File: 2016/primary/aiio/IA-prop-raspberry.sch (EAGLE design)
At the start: 94 parts, among them U1 ARDUINO_R3_SHIELD

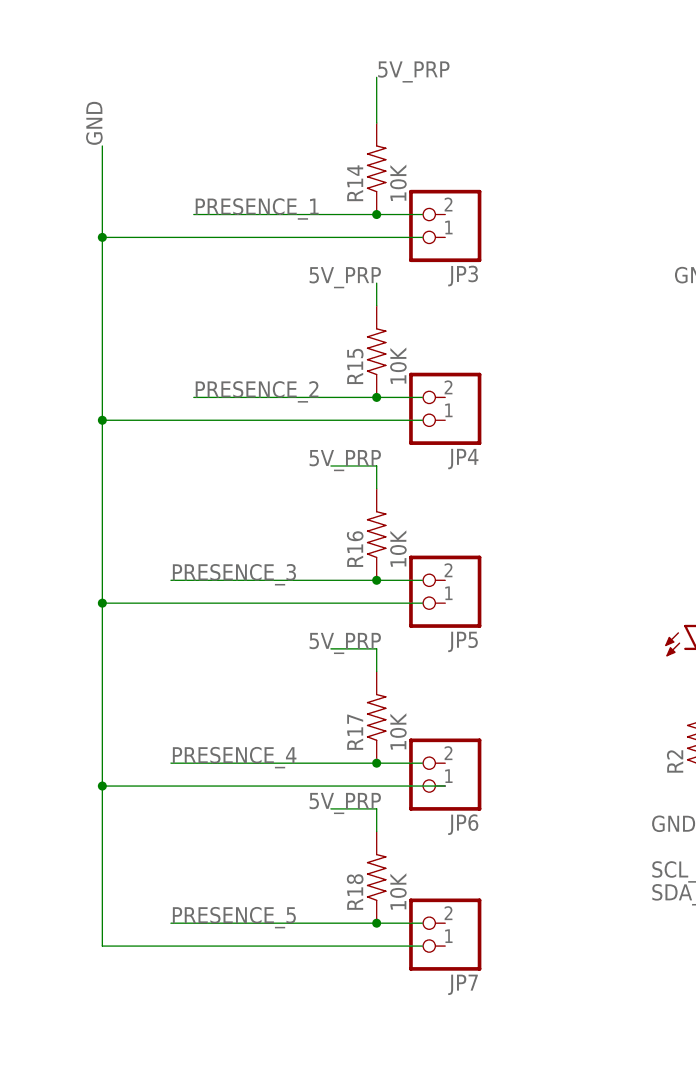
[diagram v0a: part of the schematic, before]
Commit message: [AIIO_boards] Route presence connectors.
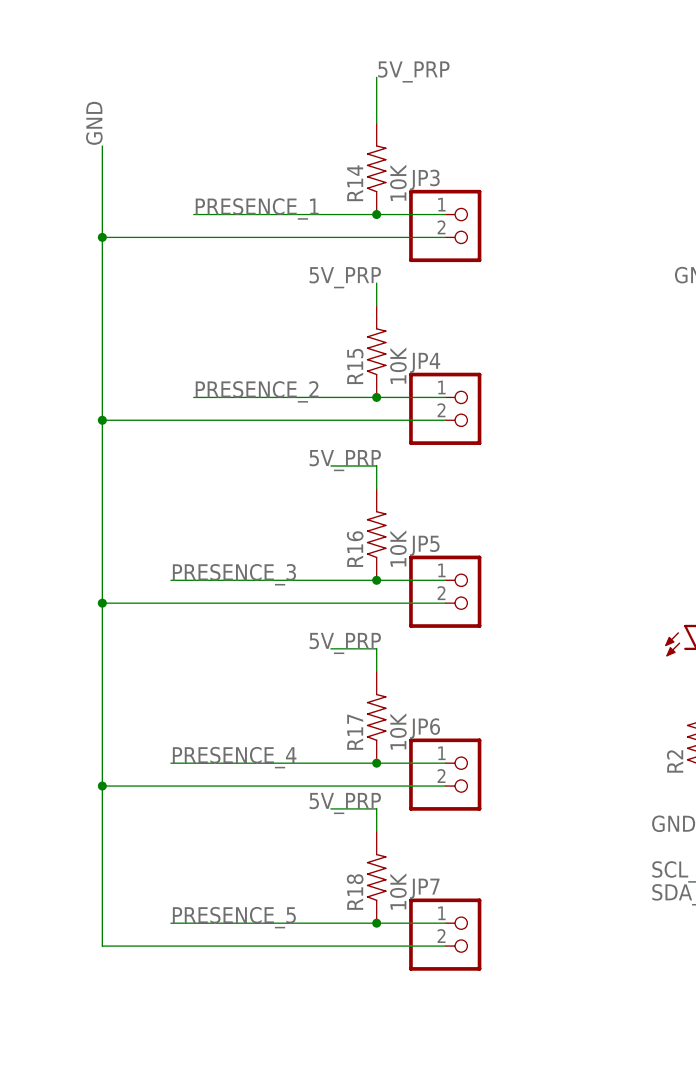
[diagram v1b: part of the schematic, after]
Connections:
- net GND: now also JP3.2, JP4.2, JP5.2, JP6.2, JP7.2; no longer JP6.1
- net PRESENCE_1: now also JP3.1
- net PRESENCE_2: now also JP4.1
- net PRESENCE_3: now also JP5.1
- net PRESENCE_4: now also JP6.1
- net PRESENCE_5: now also JP7.1
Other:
- moved on the sheet: JP3, JP4, JP5, JP6, JP7

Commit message: [AIIO_board] Add I2C and UART connectors to Arduino and RP2 boards.
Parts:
- removed ARD_BLUETOOTH: (no value), con-lstb:MA04-1
- removed CON_I2C_UART: (no value), con-lsta:FE06-1
- removed RST_RP2: (no value), SparkFun:TAC_SWITCHPTH
- added 12V_PROPU_SRC2, 12V_PROPU_SRC3, 5V_SIG, 5V_SIG2, 5V_SIG3: (no value), con-ptr500:AK300/2
- added CON_I2CARDU, CON_I2CARDU_1, CON_I2CRP2, CON_I2CRP2_2, CON_I2C_SERVOS, CON_I2C_SONARS, CON_UARTARDU, CON_UARTRP2: (no value), pinhead:PINHD-1X4
- added JP8, JP9, JP_5VSIG, JP_GND_5VSIG: (no value), pinhead:PINHD-1X3
- JP1, JP2: device SparkFun:M05PTH -> pinhead:PINHD-1X3
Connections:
- net 5V_SAL renamed 5V_PWR
- removed net N$11: 12V_PROPU_SRC-1.KL, 12V_PROPU_SRC1-1.KL, LED4.A, U$6.P$2
- removed net N$48: RP2.RUN1, RST_RP2.1
- removed net SCL_RP2: RP2.SCL, SV1.3, SV10.3, SV11.3, SV12.3, SV2.3, SV3.3, SV4.3, SV5.3, SV6.3, SV7.3, SV8.3, SV9-1.3, SV9.3
- removed net SDA_RP2: RP2.SDA, SV1.4, SV10.4, SV11.4, SV12.4, SV2.4, SV3.4, SV4.4, SV5.4, SV6.4, SV7.4, SV8.4, SV9-1.4, SV9.4
- new net 5VI2CARDU: CON_I2CARDU.4, CON_I2CARDU_1.4, JP9.3
- new net 5VI2CRP2: CON_I2CRP2.4, CON_I2CRP2_2.4, JP8.3
- new net 5VSIG: R13.2
- new net 5VSIG_SERVOS: CON_I2C_SERVOS.4, R4.2, R7.2, U$1.VDD
- new net 5VUARTRP2: CON_UARTRP2.4, JP2.1
- new net 5V_SIG: 5V_SIG-2.KL, 5V_SIG2-2.KL, 5V_SIG3-2.KL, C4.+, JP1.2, JP2.2, JP8.2, JP9.2, JP_5VSIG.1, JP_5VSIG.2, JP_5VSIG.3, LED1.A, R11.2, R12.2, R14.2, R5.1, RP2.5V0A, U$2.+VOUT, U1.5V
- new net 5V_SONARS: CON_I2C_SONARS.4, SV1.5, SV10.5, SV11.5, SV12.5, SV2.5, SV3.5, SV4.5, SV5.5, SV6.5, SV7.5, SV8.5, SV9-1.5, SV9.5
- new net GND1: CON_I2CRP2.3, CON_I2CRP2_2.3, R2.1
- new net GND2: CON_I2CARDU.3, CON_I2CARDU_1.3, U1.GND@0, U1.GND@1, U1.GND@2
- new net GND_SONARS: CON_I2C_SONARS.3, SV1.1, SV10.1, SV11.1, SV12.1, SV2.1, SV3.1, SV4.1, SV5.1, SV6.1, SV7.1, SV8.1, SV9-1.1, SV9.1
- new net N$40: 12V_PROPU_SRC-1.KL, 12V_PROPU_SRC1-1.KL, 12V_PROPU_SRC2-1.KL, 12V_PROPU_SRC3-1.KL, LED4.A, U$6.P$2
- new net SCL_RP1: CON_I2CRP2.1, CON_I2CRP2_2.1, RP2.SCL
- new net SCL_SERVOS: CON_I2C_SERVOS.1, P-UP_SCL.2, U$1.SCL
- new net SCL_SONARS: CON_I2C_SONARS.2, SV1.3, SV10.3, SV11.3, SV12.3, SV2.3, SV3.3, SV4.3, SV5.3, SV6.3, SV7.3, SV8.3, SV9-1.3, SV9.3
- new net SDA_RP1: CON_I2CRP2.2, CON_I2CRP2_2.2, RP2.SDA
- new net SDA_SERVOS: CON_I2C_SERVOS.2, P-UP_SDA.1, U$1.SDA
- new net SDA_SONARS: CON_I2C_SONARS.1, SV1.4, SV10.4, SV11.4, SV12.4, SV2.4, SV3.4, SV4.4, SV5.4, SV6.4, SV7.4, SV8.4, SV9-1.4, SV9.4
- net 5V_PRP: no longer ARD_BLUETOOTH.1, C4.+, CON_I2C_UART.1, JP1.1, JP1.2, JP1.3, JP1.4, JP1.5, LED1.A, R11.2, R12.2, R13.2, R14.2, R4.2, R5.1, R7.2, RP2.5V0A, SV1.5, SV10.5, SV11.5, SV12.5, SV2.5, SV3.5, SV4.5, SV5.5, SV6.5, SV7.5, SV8.5, SV9-1.5, SV9.5, U$1.VDD, U$2.+VOUT, U1.5V
- net ARD_RX: now also CON_UARTARDU.1; no longer ARD_BLUETOOTH.3
- net ARD_TX: now also CON_UARTARDU.2; no longer ARD_BLUETOOTH.4
- net BAT_12V_PROPU-: now also 12V_PROPU_SRC2-2.KL, 12V_PROPU_SRC3-2.KL
- net GND: now also 5V_SIG-1.KL, 5V_SIG2-1.KL, 5V_SIG3-1.KL, CON_I2C_SERVOS.3, CON_UARTARDU.3, CON_UARTRP2.3, JP_GND_5VSIG.1, JP_GND_5VSIG.2, JP_GND_5VSIG.3; no longer ARD_BLUETOOTH.2, CON_I2C_UART.2, JP2.1, JP2.2, JP2.3, JP2.4, JP2.5, R2.1, SV1.1, SV10.1, SV11.1, SV12.1, SV2.1, SV3.1, SV4.1, SV5.1, SV6.1, SV7.1, SV8.1, SV9-1.1, SV9.1, U1.GND@0, U1.GND@1, U1.GND@2
- net N$1: now also CON_UARTARDU.4, JP1.1; no longer RP2.RUN2, RST_RP2.3
- net RX_RP2: now also CON_UARTRP2.1; no longer CON_I2C_UART.6
- net SCL_ARDU: now also CON_I2CARDU.1, CON_I2CARDU_1.1; no longer CON_I2C_UART.4, P-UP_SCL.2, U$1.SCL
- net SDA_ARDU: now also CON_I2CARDU.2, CON_I2CARDU_1.2; no longer CON_I2C_UART.3, P-UP_SDA.1, U$1.SDA
- net TX_RP2: now also CON_UARTRP2.2; no longer CON_I2C_UART.5
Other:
- moved on the sheet: 12V_BOARDS1-1, 12V_BOARDS1-2, C3, C4, IHM, LED1, LED2, LED3, P-UP_SCL, P-UP_SDA, PWR_RP2, R1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

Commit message: [AIIO_board] Route IHM components.
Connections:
- removed net GND2: CON_I2CARDU.3, CON_I2CARDU_1.3, U1.GND@0, U1.GND@1, U1.GND@2
- removed net GND_SONARS: CON_I2C_SONARS.3, SV1.1, SV10.1, SV11.1, SV12.1, SV2.1, SV3.1, SV4.1, SV5.1, SV6.1, SV7.1, SV8.1, SV9-1.1, SV9.1
- net GND: now also CON_I2CARDU.3, CON_I2CARDU_1.3, CON_I2C_SONARS.3, SV1.1, SV10.1, SV11.1, SV12.1, SV2.1, SV3.1, SV4.1, SV5.1, SV6.1, SV7.1, SV8.1, SV9-1.1, SV9.1, U1.GND@0, U1.GND@1, U1.GND@2
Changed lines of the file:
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@@
 <label x="269.24" y="-91.44" size="1.778" layer="95"/>
+</segment>
+<segment>
+<pinref part="SV3" gate="G$1" pin="1"/>
+<wire x1="320.04" y1="55.88" x2="322.58" y2="55.88" width="0.1524" layer="91"/>
+<wire x1="322.58" y1="55.88" x2="322.58" y2="30.48" width="0.1524" layer="91"/>
+<pinref part="SV2" gate="G$1" pin="1"/>
+<wire x1="322.58" y1="30.48" x2="322.58" y2="2.54" width="0.1524" layer="91"/>
+<wire x1="322.58" y1="2.54" x2="322.58" y2="-25.4" width="0.1524" layer="91"/>
+<wire x1="322.58" y1="-25.4" x2="322.58" y2="-43.18" width="0.1524" layer="91"/>
+<wire x1="294.64" y1="55.88" x2="297.18" y2="55.88" width="0.1524" layer="91"/>
+<wire x1="297.18" y1="55.88" x2="297.18" y2="30.48" width="0.1524" layer="91"/>
+<wire x1="297.18" y1="30.48" x2="297.18" y2="2.54" width="0.1524" layer="91"/>
+<wire x1="297.18" y1="2.54" x2="297.18" y2="-25.4" width="0.1524" layer="91"/>
+<wire x1="297.18" y1="-25.4" x2="297.18" y2="-43.18" width="0.1524" layer="91"/>
+<wire x1="322.58" y1="-43.18" x2="297.18" y2="-43.18" width="0.1524" layer="91"/>
+<pinref part="SV1" gate="G$1" pin="1"/>
+<wire x1="269.24" y1="55.88" x2="271.78" y2="55.88" width="0.1524" layer="91"/>
+<wire x1="271.78" y1="55.88" x2="271.78" y2="30.48" width="0.1524" layer="91"/>
+<pinref part="SV4" gate="G$1" pin="1"/>
+<wire x1="271.78" y1="30.48" x2="271.78" y2="2.54" width="0.1524" layer="91"/>
+<wire x1="271.78" y1="2.54" x2="271.78" y2="-25.4" width="0.1524" layer="91"/>
+<wire x1="271.78" y1="-25.4" x2="271.78" y2="-43.18" width="0.1524" layer="91"/>
+<wire x1="269.24" y1="30.48" x2="271.78" y2="30.48" width="0.1524" layer="91"/>
+<junction x="271.78" y="30.48"/>
+<pinref part="SV7" gate="G$1" pin="1"/>
+<wire x1="269.24" y1="2.54" x2="271.78" y2="2.54" width="0.1524" layer="91"/>
+<junction x="271.78" y="2.54"/>
+<pinref part="SV10" gate="G$1" pin="1"/>
+<wire x1="269.24" y1="-25.4" x2="271.78" y2="-25.4" width="0.1524" layer="91"/>
+<junction x="271.78" y="-25.4"/>
+<wire x1="297.18" y1="-43.18" x2="271.78" y2="-43.18" width="0.1524" layer="91"/>
+<junction x="297.18" y="-43.18"/>
+<wire x1="271.78" y1="-43.18" x2="261.62" y2="-43.18" width="0.1524" layer="91"/>
+<junction x="271.78" y="-43.18"/>
+<label x="251.46" y="-43.18" size="1.778" layer="95"/>
+<pinref part="SV5" gate="G$1" pin="1"/>
+<wire x1="294.64" y1="30.48" x2="297.18" y2="30.48" width="0.1524" layer="91"/>
+<junction x="297.18" y="30.48"/>
+<pinref part="SV8" gate="G$1" pin="1"/>
+<wire x1="294.64" y1="2.54" x2="297.18" y2="2.54" width="0.1524" layer="91"/>
+<junction x="297.18" y="2.54"/>
+<pinref part="SV6" gate="G$1" pin="1"/>
+<wire x1="320.04" y1="30.48" x2="322.58" y2="30.48" width="0.1524" layer="91"/>
+<junction x="322.58" y="30.48"/>
+<pinref part="SV9" gate="G$1" pin="1"/>
+<wire x1="320.04" y1="2.54" x2="322.58" y2="2.54" width="0.1524" layer="91"/>
+<junction x="322.58" y="2.54"/>
+<pinref part="SV12" gate="G$1" pin="1"/>
+<wire x1="320.04" y1="-25.4" x2="322.58" y2="-25.4" width="0.1524" layer="91"/>
+<junction x="322.58" y="-25.4"/>
+<pinref part="SV9-1" gate="G$1" pin="1"/>
+<wire x1="335.28" y1="2.54" x2="322.58" y2="2.54" width="0.1524" layer="91"/>
+<pinref part="SV11" gate="G$1" pin="1"/>
+<wire x1="294.64" y1="-25.4" x2="297.18" y2="-25.4" width="0.1524" layer="91"/>
+<junction x="297.18" y="-25.4"/>
+<pinref part="CON_I2C_SONARS" gate="A" pin="3"/>
+</segment>
+<segment>
+<pinref part="CON_I2CARDU_1" gate="A" pin="3"/>
+<wire x1="172.72" y1="-127" x2="193.04" y2="-127" width="0.1524" layer="91"/>
+<pinref part="CON_I2CARDU" gate="A" pin="3"/>
+<wire x1="172.72" y1="-144.78" x2="193.04" y2="-144.78" width="0.1524" layer="91"/>
+<wire x1="193.04" y1="-144.78" x2="198.12" y2="-144.78" width="0.1524" layer="91"/>
+<wire x1="193.04" y1="-127" x2="193.04" y2="-144.78" width="0.1524" layer="91"/>
+<junction x="193.04" y="-144.78"/>
+<wire x1="198.12" y1="-144.78" x2="198.12" y2="-127" width="0.1524" layer="91"/>
+<pinref part="U1" gate="G$1" pin="GND@2"/>
+<wire x1="220.98" y1="-124.46" x2="215.9" y2="-124.46" width="0.1524" layer="91"/>
+<pinref part="U1" gate="G$1" pin="GND@1"/>
+<wire x1="220.98" y1="-127" x2="215.9" y2="-127" width="0.1524" layer="91"/>
+<wire x1="215.9" y1="-127" x2="215.9" y2="-124.46" width="0.1524" layer="91"/>
+<wire x1="215.9" y1="-127" x2="215.9" y2="-129.54" width="0.1524" layer="91"/>
+<junction x="215.9" y="-127"/>
+<pinref part="U1" gate="G$1" pin="GND@0"/>
+<wire x1="215.9" y1="-129.54" x2="220.98" y2="-129.54" width="0.1524" layer="91"/>
+<wire x1="215.9" y1="-129.54" x2="215.9" y2="-132.08" width="0.1524" layer="91"/>
+<junction x="215.9" y="-129.54"/>
+<label x="213.36" y="-134.62" size="1.778" layer="95"/>
+<wire x1="198.12" y1="-127" x2="215.9" y2="-127" width="0.1524" layer="91"/>
 </segment>
 </net>
@@
 <wire x1="58.42" y1="-104.14" x2="58.42" y2="-121.92" width="0.1524" layer="91"/>
 <junction x="58.42" y="-121.92"/>
-</segment>
-</net>
-<net name="GND2" class="0">
-<segment>
-<pinref part="CON_I2CARDU_1" gate="A" pin="3"/>
-<wire x1="172.72" y1="-127" x2="193.04" y2="-127" width="0.1524" layer="91"/>
-<pinref part="CON_I2CARDU" gate="A" pin="3"/>
-<wire x1="172.72" y1="-144.78" x2="193.04" y2="-144.78" width="0.1524" layer="91"/>
-<wire x1="193.04" y1="-144.78" x2="198.12" y2="-144.78" width="0.1524" layer="91"/>
-<wire x1="193.04" y1="-127" x2="193.04" y2="-144.78" width="0.1524" layer="91"/>
-<junction x="193.04" y="-144.78"/>
-<wire x1="198.12" y1="-144.78" x2="198.12" y2="-127" width="0.1524" layer="91"/>
-<pinref part="U1" gate="G$1" pin="GND@2"/>
-<wire x1="220.98" y1="-124.46" x2="215.9" y2="-124.46" width="0.1524" layer="91"/>
-<pinref part="U1" gate="G$1" pin="GND@1"/>
-<wire x1="220.98" y1="-127" x2="215.9" y2="-127" width="0.1524" layer="91"/>
-<wire x1="215.9" y1="-127" x2="215.9" y2="-124.46" width="0.1524" layer="91"/>
-<wire x1="215.9" y1="-127" x2="215.9" y2="-129.54" width="0.1524" layer="91"/>
-<junction x="215.9" y="-127"/>
-<pinref part="U1" gate="G$1" pin="GND@0"/>
-<wire x1="215.9" y1="-129.54" x2="220.98" y2="-129.54" width="0.1524" layer="91"/>
-<wire x1="215.9" y1="-129.54" x2="215.9" y2="-132.08" width="0.1524" layer="91"/>
-<junction x="215.9" y="-129.54"/>
-<label x="213.36" y="-134.62" size="1.778" layer="95"/>
-<wire x1="198.12" y1="-127" x2="215.9" y2="-127" width="0.1524" layer="91"/>
 </segment>
 </net>
@@
 </segment>
 </net>
-<net name="GND_SONARS" class="0">
-<segment>
-<pinref part="SV3" gate="G$1" pin="1"/>
-<wire x1="320.04" y1="55.88" x2="322.58" y2="55.88" width="0.1524" layer="91"/>
-<wire x1="322.58" y1="55.88" x2="322.58" y2="30.48" width="0.1524" layer="91"/>
-<pinref part="SV2" gate="G$1" pin="1"/>
-<wire x1="322.58" y1="30.48" x2="322.58" y2="2.54" width="0.1524" layer="91"/>
-<wire x1="322.58" y1="2.54" x2="322.58" y2="-25.4" width="0.1524" layer="91"/>
-<wire x1="322.58" y1="-25.4" x2="322.58" y2="-43.18" width="0.1524" layer="91"/>
-<wire x1="294.64" y1="55.88" x2="297.18" y2="55.88" width="0.1524" layer="91"/>
-<wire x1="297.18" y1="55.88" x2="297.18" y2="30.48" width="0.1524" layer="91"/>
-<wire x1="297.18" y1="30.48" x2="297.18" y2="2.54" width="0.1524" layer="91"/>
-<wire x1="297.18" y1="2.54" x2="297.18" y2="-25.4" width="0.1524" layer="91"/>
-<wire x1="297.18" y1="-25.4" x2="297.18" y2="-43.18" width="0.1524" layer="91"/>
-<wire x1="322.58" y1="-43.18" x2="297.18" y2="-43.18" width="0.1524" layer="91"/>
-<pinref part="SV1" gate="G$1" pin="1"/>
-<wire x1="269.24" y1="55.88" x2="271.78" y2="55.88" width="0.1524" layer="91"/>
-<wire x1="271.78" y1="55.88" x2="271.78" y2="30.48" width="0.1524" layer="91"/>
-<pinref part="SV4" gate="G$1" pin="1"/>
-<wire x1="271.78" y1="30.48" x2="271.78" y2="2.54" width="0.1524" layer="91"/>
-<wire x1="271.78" y1="2.54" x2="271.78" y2="-25.4" width="0.1524" layer="91"/>
-<wire x1="271.78" y1="-25.4" x2="271.78" y2="-43.18" width="0.1524" layer="91"/>
-<wire x1="269.24" y1="30.48" x2="271.78" y2="30.48" width="0.1524" layer="91"/>
-<junction x="271.78" y="30.48"/>
-<pinref part="SV7" gate="G$1" pin="1"/>
-<wire x1="269.24" y1="2.54" x2="271.78" y2="2.54" width="0.1524" layer="91"/>
-<junction x="271.78" y="2.54"/>
-<pinref part="SV10" gate="G$1" pin="1"/>
-<wire x1="269.24" y1="-25.4" x2="271.78" y2="-25.4" width="0.1524" layer="91"/>
-<junction x="271.78" y="-25.4"/>
-<wire x1="297.18" y1="-43.18" x2="271.78" y2="-43.18" width="0.1524" layer="91"/>
-<junction x="297.18" y="-43.18"/>
-<wire x1="271.78" y1="-43.18" x2="261.62" y2="-43.18" width="0.1524" layer="91"/>
-<junction x="271.78" y="-43.18"/>
-<label x="241.3" y="-43.18" size="1.778" layer="95"/>
-<pinref part="SV5" gate="G$1" pin="1"/>
-<wire x1="294.64" y1="30.48" x2="297.18" y2="30.48" width="0.1524" layer="91"/>
-<junction x="297.18" y="30.48"/>
-<pinref part="SV8" gate="G$1" pin="1"/>
-<wire x1="294.64" y1="2.54" x2="297.18" y2="2.54" width="0.1524" layer="91"/>
-<junction x="297.18" y="2.54"/>
-<pinref part="SV6" gate="G$1" pin="1"/>
-<wire x1="320.04" y1="30.48" x2="322.58" y2="30.48" width="0.1524" layer="91"/>
-<junction x="322.58" y="30.48"/>
-<pinref part="SV9" gate="G$1" pin="1"/>
-<wire x1="320.04" y1="2.54" x2="322.58" y2="2.54" width="0.1524" layer="91"/>
-<junction x="322.58" y="2.54"/>
-<pinref part="SV12" gate="G$1" pin="1"/>
-<wire x1="320.04" y1="-25.4" x2="322.58" y2="-25.4" width="0.1524" layer="91"/>
-<junction x="322.58" y="-25.4"/>
-<pinref part="SV9-1" gate="G$1" pin="1"/>
-<wire x1="335.28" y1="2.54" x2="322.58" y2="2.54" width="0.1524" layer="91"/>
-<pinref part="SV11" gate="G$1" pin="1"/>
-<wire x1="294.64" y1="-25.4" x2="297.18" y2="-25.4" width="0.1524" layer="91"/>
-<junction x="297.18" y="-25.4"/>
-<pinref part="CON_I2C_SONARS" gate="A" pin="3"/>
-</segment>
-</net>
